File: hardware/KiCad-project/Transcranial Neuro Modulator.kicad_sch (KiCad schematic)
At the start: 59 parts, among them U1 ADA4528, U2 Mikroe Boost 8 Click, U3 ST Nucleo U575ZI-Q board, U4 Mikroe DAC 9 Click, U5 Active Buzzer Module, U6 ADA4528, U7 OPA569, U8 OPA569

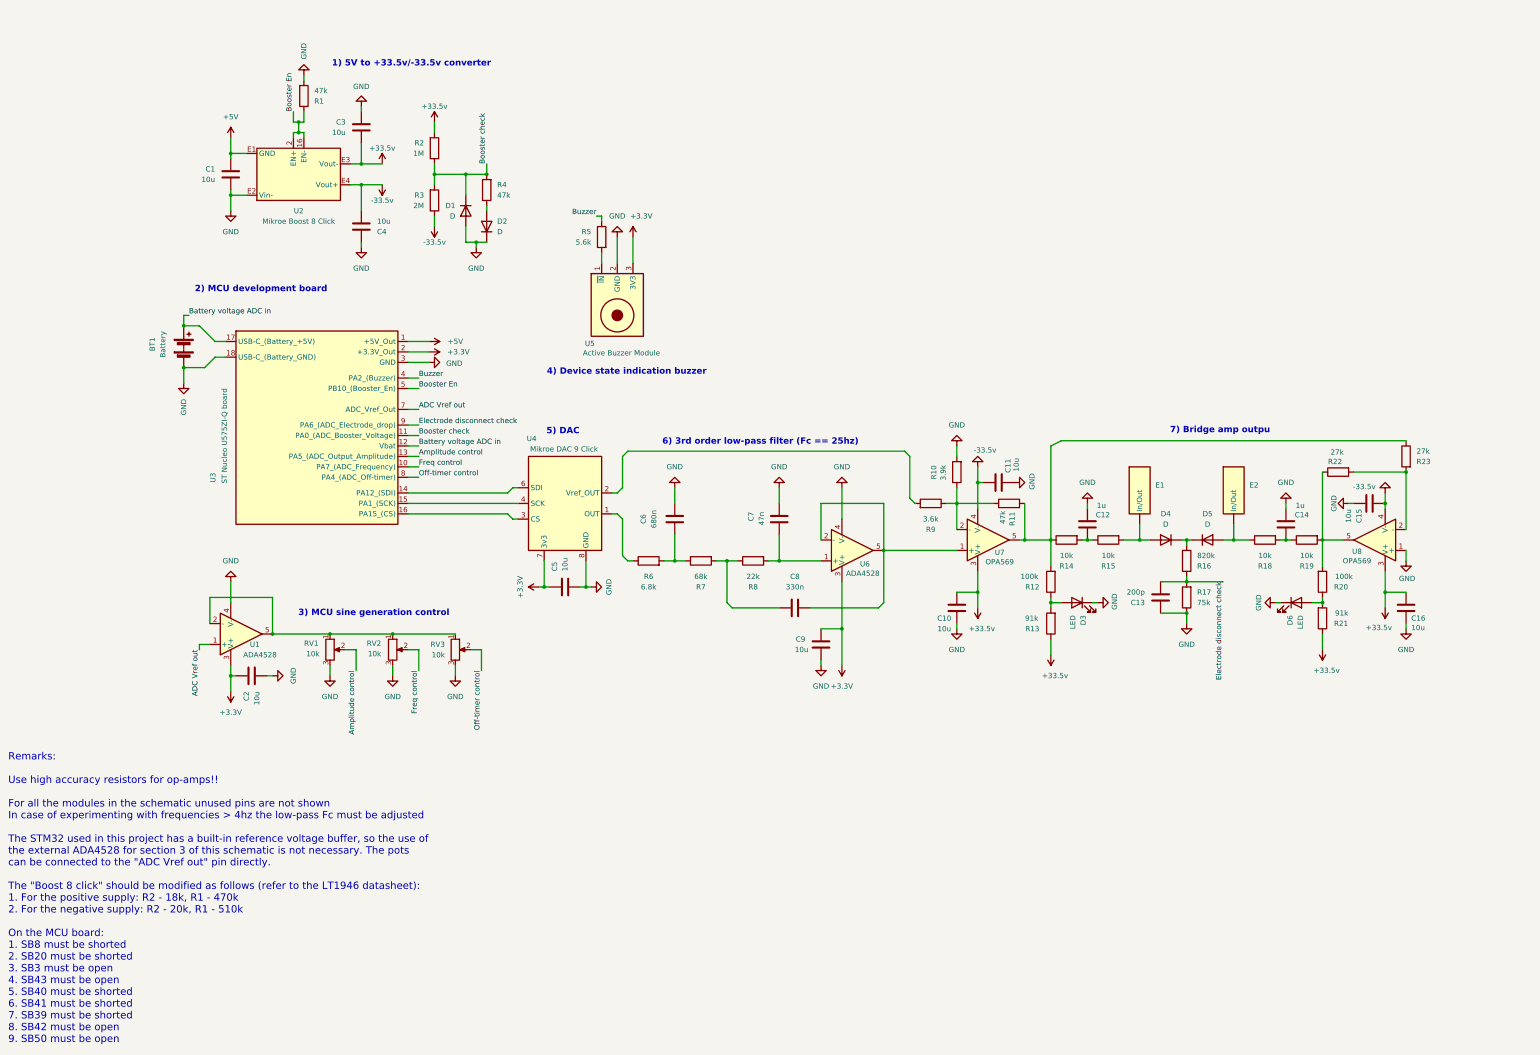
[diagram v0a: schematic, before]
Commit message: Add files via upload
Next version. Current source added; DC protection added... Plus a number of other major reworks.
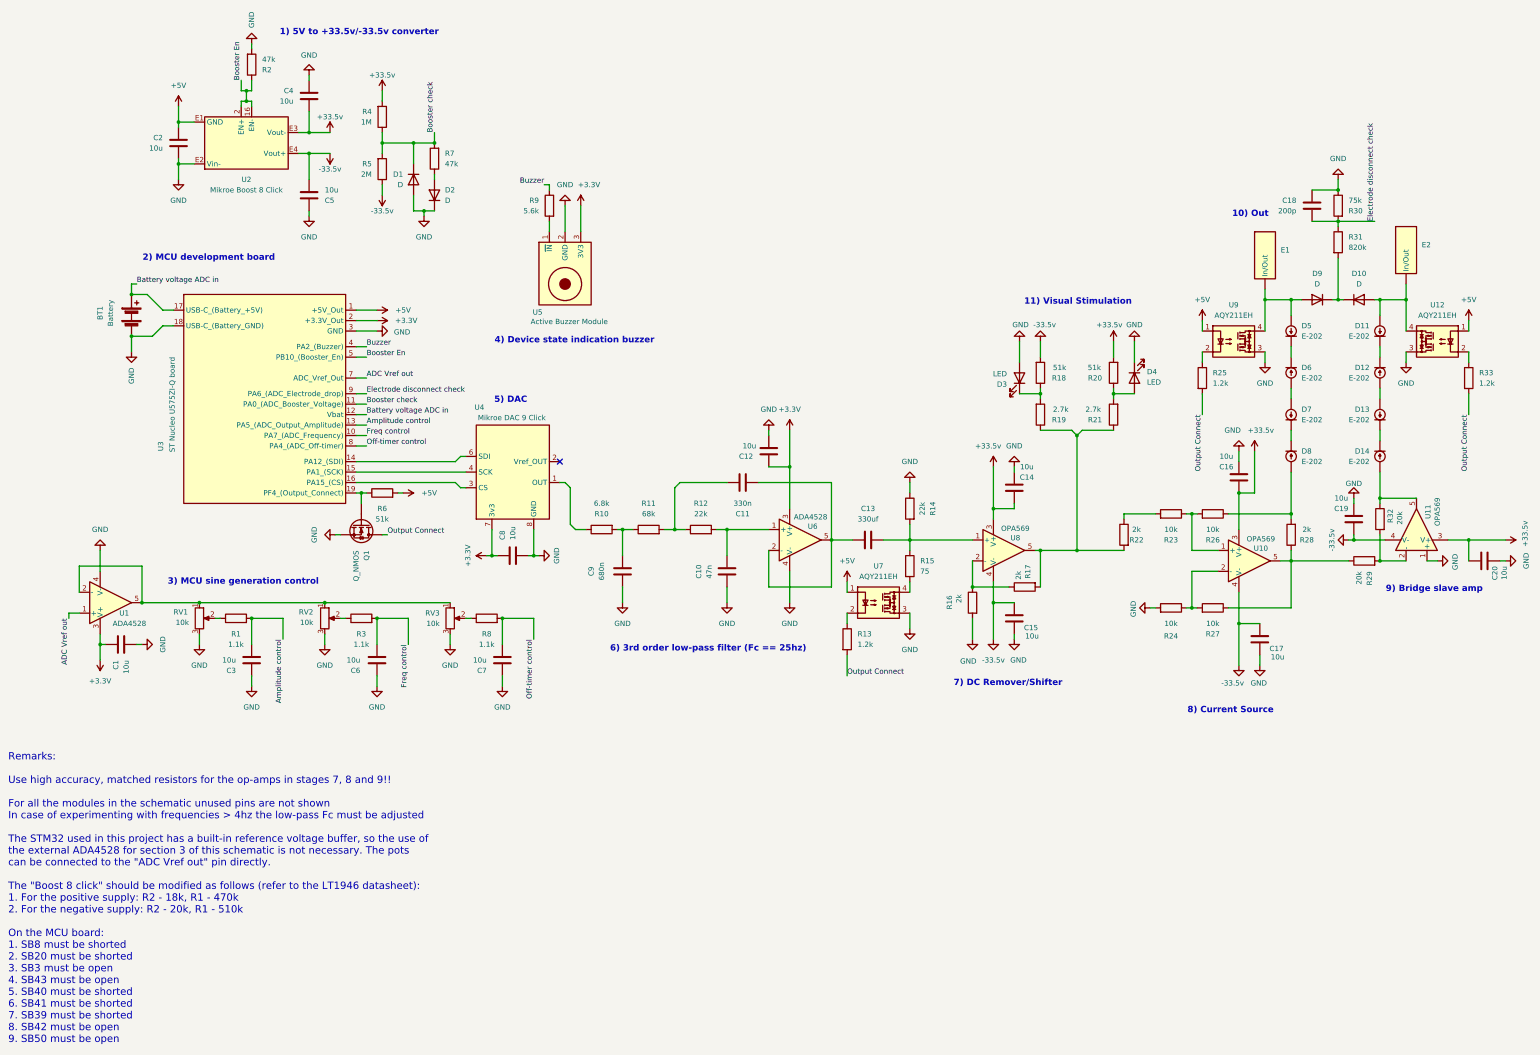
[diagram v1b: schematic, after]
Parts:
- removed C12, C14: 1u, symbol Device:C
- removed R18, R19: 10k, symbol Device:R
- removed R9: 3.6k, symbol Device:R
- added C13: 330uf, symbol Device:C
- added C16, C17, C3, C6, C7: 10u, symbol Device:C
- added D11, D12, D13, D14, D5, D6, D7, D8: E-202, symbol Device:D_Current-regulator
- added Q1: Q_NMOS, symbol Device:Q_NMOS
- added R1, R3, R8: 1.1k, symbol Device:R
- added R13, R25, R33: 1.2k, symbol Device:R
- added R22, R28: 2k, symbol Device:R
- added R23, R24, R26, R27: 10k, symbol Device:R
- added R6: 51k, symbol Device:R
- added U10: OPA569, symbol Simulation_SPICE:OPAMP
- added U12, U7, U9: AQY211EH, Package_DIP:DIP-4_W7.62mm, symbol Relay_SolidState:TLP222A
- R14: value 10k -> 22k
- R15: value 10k -> 75
- R16: renamed from R10; value 3.9k -> 2k
- R17: renamed from R11; value 47k -> 2k
- R18: renamed from R12; value 100k -> 51k
- R19: renamed from R13; value 91k -> 2.7k
- R20: value 100k -> 51k
- R21: value 91k -> 2.7k
- R29: renamed from R23; value 27k -> 20k
- R32: renamed from R22; value 27k -> 20k
- renumbered C2 to C1, C7 to C10, C8 to C11, C9 to C12, C10 to C14, C11 to C15, C13 to C18, C15 to C19, C1 to C2, C16 to C20, C3 to C4, C4 to C5, C5 to C8, C6 to C9, D5 to D10, D6 to D4, D4 to D9, R6 to R10, R7 to R11, R8 to R12, R1 to R2, R17 to R30, R16 to R31, R2 to R4, R3 to R5, R4 to R7, R5 to R9, U8 to U11, U7 to U8
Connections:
- net +33.5v: now also R20.2, C16.1, U10.3 (V+); no longer R19.1, R21.1
- net +5V: now also R6.2, U12.1, U7.1, U9.1
- net -33.5v: now also R18.2, C17.1, U10.4 (V-)
- net Amplitude control: now also C3.2, R1.2; no longer RV1.2
- net Freq control: now also C6.2, R3.2; no longer RV2.2
- net GND: now also D3.2 (A), R14.1, C16.2, C17.2, C3.1, C6.1, C7.1, Q1.S, R24.2, U12.3, U7.3, U9.3; no longer D3.1 (K)
- net Off-timer control: now also C7.2, R8.2; no longer RV3.2
- net at C11.2, U6.2 (-), U6.5: now also C13.2; no longer U8.1 (+)
- net at D9.2 (A), E1. (In/Out): now also D5.2 (A), U9.4; no longer R15.2
- net at R32.1, U11.5: now also D14.2 (A); no longer R20.2
- net at R14.2, R15.1: now also U8.1 (+), C13.1
- net at R18.1, R19.2: now also D3.1 (K); no longer D3.2 (A)
- net at D10.2 (A), E2. (In/Out): now also D11.2 (A), U12.4
- new net: Q1.G, R6.1, U3.19 (PF4_(Output_Connect))
- new net: D8.2 (A), R26.1, R28.2
- new net: R23.1, R26.2, U10.1 (+)
- new net: D5.1 (K), D6.1 (K)
- new net: D6.2 (A), D7.2 (A)
- new net: R25.1, U9.2
- new net: R27.1, R28.1, R29.1, U10.5
- new net: R1.1, RV1.2
- new net: R22.1, R23.2
- new net: R17.2, R19.1, R21.1, R22.2, U8.5
- new net: R3.1, RV2.2
- new net: D7.1 (K), D8.1 (K)
- new net: R15.2, U7.4
- new net: D13.1 (K), D14.1 (K)
- new net: D12.2 (A), D13.2 (A)
- new net: R8.1, RV3.2
- new net: R33.1, U12.2
- new net: R13.1, U7.2
- new net: R24.1, R27.2, U10.2 (-)
- new net: D11.1 (K), D12.1 (K)
- new net Output Connect: Q1.D, R13.2, R25.2, R33.2
- no-connect marks 0 -> 1
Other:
- note added: "10) Out"
- note added: "11) Visual Stimulation"
- note added: "7) DC Remover/Shifter"
- note added: "8) Current Source"
- note added: "9) Bridge slave amp"
- note added: "Remarks: Use high accuracy, matched resistors for the op-amps in stages 7, 8 and 9!! For all the modules in the schematic unused pins are not shown In case of experimenting with frequencies > 4hz the low-pass Fc must be adjusted The STM32 used in this project has a built-in reference voltage buffer, so the use of the external ADA4528 for section 3 of this schematic is not necessary. The pots can 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"
- note removed: "7) Bridge amp outpu"
- note removed: "Remarks: Use high accuracy resistors for op-amps!! For all the modules in the schematic unused pins are not shown In case of experimenting with frequencies > 4hz the low-pass Fc must be adjusted The STM32 used in this project has a built-in reference voltage buffer, so the use of the external ADA4528 for section 3 of this schematic is not necessary. The pots can be connected to the "ADC Vref out"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"
- moved on the sheet: BT1, C1, C10, C11, C12, C14, C15, C18, C19, C2, C20, C4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
